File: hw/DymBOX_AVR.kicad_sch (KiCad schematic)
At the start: 45 parts, among them J4 DS18B20, J5 Conn_02x05_Odd_Even, J6 Conn_01x01_Pin, J7 Conn_01x01_Pin, J8 Conn_01x01_Pin, J9 Conn_01x01_Pin, K1 RT314A24, Q1 BC327, Q2 BC327, Q3 BS170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

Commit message: prace
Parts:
- removed J7, J8, J9: Conn_01x01_Pin, 2pkstartup:TRM2_62409-1_TEC, symbol 2pkstartup:FST
- added J1, J2, J3: Conn_01x01_Pin, 2pkstartup:faston_6.3, symbol 2pkstartup:FST
- J6: footprint 2pkstartup:TRM2_62409-1_TEC -> 2pkstartup:faston_6.3
- SW1: footprint Rotary_Encoder:RotaryEncoder_Alps_EC12E-Switch_Vertical_H20mm_CircularMountingHoles -> 2pkstartup:RotaryEncoder_Alps_EC12E-Switch_Vertical_H20mm_CircularMountingHoles
- U3: footprint Package_TO_SOT_THT:TO-220-3_Horizontal_TabDown -> Package_TO_SOT_THT:TO-220-3_Vertical
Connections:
- net at K1.11: now also J3.1 (Pin_1)
- net at TR1.5: now also J1.1 (Pin_1); no longer J6.1 (Pin_1)
- net at TR1.1: now also J2.1 (Pin_1)
- net at K1.14: now also J6.1 (Pin_1)

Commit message: uprava a více
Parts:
- removed J4: DS18B20, Connector_Wire:SolderWire-0.127sqmm_1x03_P3.7mm_D0.48mm_OD1mm, symbol Connector:Conn_01x03_Pin
- removed SW1: RotaryEncoder_Switch, 2pkstartup:RotaryEncoder_Alps_EC12E-Switch_Vertical_H20mm_CircularMountingHoles, symbol Device:RotaryEncoder_Switch
- added J4: Screw_Terminal_01x03, TerminalBlock_Phoenix:TerminalBlock_Phoenix_PT-1,5-3-3.5-H_1x03_P3.50mm_Horizontal, symbol Connector:Screw_Terminal_01x03
- added J7: Screw_Terminal_01x02, TerminalBlock_Phoenix:TerminalBlock_Phoenix_PT-1,5-2-3.5-H_1x02_P3.50mm_Horizontal, symbol Connector:Screw_Terminal_01x02
- added SW2: RotaryEncoder_Switch, 2pkstartup:RotaryEncoder_Alps_EC12E-Switch_Vertical_H20mm_CircularMountingHoles, symbol 2pkstartup:RotaryEncoder_Switch
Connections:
- net +12V: now also J7.1 (Pin_1)
- net +5V: now also J4.3 (Pin_3)
- net BTN: now also SW2.S1
- net CLK: now also SW2.A
- net DT: now also SW2.B
- net GND: now also J4.1 (Pin_1), SW2.C, SW2.S2
- net at D1.2 (A), Q3.1 (D): now also J7.2 (Pin_2)
- net at R13.1, U1.28 (PC5): now also J4.2 (Pin_2)
- net at Q1.1 (C): now also U2.8 (CA3); no longer U2.6 (CA4)
- net at Q2.1 (C): now also U2.9 (CA2); no longer U2.8 (CA3)
- net at Q5.1 (C): now also U2.12 (CA1); no longer U2.9 (CA2)
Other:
- moved on the sheet: Q1, Q2, Q5, R11, R12

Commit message: AP63005
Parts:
- removed U2: CA56-12EWA, Display_7Segment:CA56-12EWA, symbol Display_Character:CA56-12EWA
- added U2: FYT-5631BUHR-21, 2pkstartup:FYT-5631BUHR-21, symbol 2pkstartup:FYT-5631BUHR-21
- C1, C2: footprint Capacitor_THT:CP_Radial_D13.0mm_P5.00mm -> Capacitor_THT:CP_Radial_D16.0mm_P7.50mm
- U3: footprint Package_TO_SOT_THT:TO-220-3_Vertical -> Package_TO_SOT_THT:TO-220-3_Horizontal_TabDown
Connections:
- net at R7.2: now also U2.3 (DPX)
- net at R6.2: now also U2.2 (d)
- net at R8.2: now also U2.10 (f)
- net at R9.2: now also U2.5 (g)
- net at R2.2: now also U2.11 (a)
- net at R3.2: now also U2.7 (b)
- net at R5.2: now also U2.1 (e)
- net at R4.2: now also U2.4 (c)
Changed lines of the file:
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@@
 			)
 		)
-		(property "Footprint" "Package_TO_SOT_THT:TO-220-3_Vertical"
+		(property "Footprint" "Package_TO_SOT_THT:TO-220-3_Horizontal_TabDown"
 			(at 53.975 64.77 0)
 			(show_name no)
@@
 			)
 		)
-		(property "Footprint" "Capacitor_THT:CP_Radial_D13.0mm_P5.00mm"
+		(property "Footprint" "Capacitor_THT:CP_Radial_D16.0mm_P7.50mm"
 			(at 40.3352 68.58 0)
 			(hide yes)
@@
 			)
 		)
-		(property "Footprint" "Capacitor_THT:CP_Radial_D13.0mm_P5.00mm"
+		(property "Footprint" "Capacitor_THT:CP_Radial_D16.0mm_P7.50mm"
 			(at 61.9252 68.58 0)
 			(hide yes)
@@
 	)
 	(symbol
-		(lib_id "Display_Character:CA56-12EWA")
-		(at 139.7 43.18 0)
-		(unit 1)
-		(body_style 1)
-		(exclude_from_sim no)
-		(in_bom yes)
-		(on_board yes)
-		(in_pos_files yes)
-		(dnp no)
-		(fields_autoplaced yes)
-		(property "Reference" "U2"
-			(at 139.7 25.4 0)
-			(show_name no)
-			(do_not_autoplace no)
-			(effects
-				(font
-					(size 1.27 1.27)
-				)
-			)
-		)
-		(property "Value" "CA56-12EWA"
-			(at 139.7 27.94 0)
-			(show_name no)
-			(do_not_autoplace no)
-			(effects
-				(font
-					(size 1.27 1.27)
-				)
-			)
-		)
-		(property "Footprint" "Display_7Segment:CA56-12EWA"
-			(at 139.7 58.42 0)
-			(hide yes)
-			(show_name no)
-			(do_not_autoplace no)
-			(effects
-				(font
-					(size 1.27 1.27)
-				)
-			)
-		)
-		(property "Datasheet" "http://www.kingbrightusa.com/images/catalog/SPEC/CA56-12EWA.pdf"
-			(at 128.778 42.418 0)
-			(hide yes)
-			(show_name no)
-			(do_not_autoplace no)
-			(effects
-				(font
-					(size 1.27 1.27)
-				)
-			)
-		)
-		(property "Description" "4 digit 7 segment high efficiency red LED, common anode"
-			(at 139.7 43.18 0)
-			(hide yes)
-			(show_name no)
-			(do_not_autoplace no)
-			(effects
-				(font
-					(size 1.27 1.27)
-				)
-			)
-		)
-		(pin "10"
-		)
-		(pin "3"
-		)
-		(pin "11"
-		)
-		(pin "9"
-		)
-		(pin "8"
-		)
-		(pin "12"
-		)
-		(pin "6"
-		)
-		(pin "4"
-		)
-		(pin "7"
-		)
-		(pin "5"
-		)
-		(pin "1"
-		)
-		(pin "2"
-		)
-		(instances
-			(project "DymBOX_AVR"
-				(path "/586f9677-488d-4753-8c82-bcf4ec642766"
-					(reference "U2")
-					(unit 1)
-				)
-			)
-		)
-	)
-	(symbol
 		(lib_id "Device:R")
 		(at 118.11 110.49 180)
@@
 					(unit 1)
 				)
+			)
+		)
+	)
+	(symbol
+		(lib_id "2pkstartup:FYT-5631BUHR-21")
+		(at 139.7 43.18 0)
+		(unit 1)
+		(body_style 1)
+		(exclude_from_sim no)
+		(in_bom yes)
+		(on_board yes)
+		(in_pos_files yes)
+		(dnp no)
+		(fields_autoplaced yes)
+		(property "Reference" "U2"
+			(at 133.985 25.4 0)
+			(show_name no)
+			(do_not_autoplace no)
+			(effects
+				(font
+					(size 1.27 1.27)
+				)
+			)
+		)
+		(property "Value" "FYT-5631BUHR-21"
+			(at 133.985 27.94 0)
+			(show_name no)
+			(do_not_autoplace no)
+			(effects
+				(font
+					(size 1.27 1.27)
+				)
+			)
+		)
+		(property "Footprint" "2pkstartup:FYT-5631BUHR-21"
+			(at 139.7 58.42 0)
+			(hide yes)
+			(show_name no)
+			(do_not_autoplace no)
+			(effects
+				(font
+					(size 1.27 1.27)
+				)
+			)
+		)
+		(property "Datasheet" "https://cetest02.cn-bj.ufileos.com/100001_2003185297/20%20FYT-5631A-BX-XX.pdf"
+			(at 128.778 42.418 0)
+			(hide yes)
+			(show_name no)
+			(do_not_autoplace no)
+			(effects
+				(font
+					(size 1.27 1.27)
+				)
+			)
+		)
+		(property "Description" "3 digit 7 segment high efficiency red LED, common anode"
+			(at 139.7 43.18 0)
+			(hide yes)
+			(show_name no)
+			(do_not_autoplace no)
+			(effects
+				(font
+					(size 1.27 1.27)
+				)
+			)
+		)
+		(pin "3"
+		)
+		(pin "1"
+		)
+		(pin "4"
+		)
+		(pin "2"
+		)
+		(pin "9"
+		)
+		(pin "5"
+		)
+		(pin "8"
+		)
+		(pin "7"
+		)
+		(pin "10"
+		)
+		(pin "6"
+		)
+		(pin "11"
+		)
+		(pin "12"
+		)
+		(instances
+			(project "DymBOX_AVR"
+				(path "/586f9677-488d-4753-8c82-bcf4ec642766"
+					(reference "U2")
+					(unit 1)
+				)

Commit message: AP63005
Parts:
- removed C1, C2: C_Polarized, Capacitor_THT:CP_Radial_D16.0mm_P7.50mm, symbol Device:C_Polarized
- removed C3: C_Small, Capacitor_THT:C_Disc_D5.0mm_W2.5mm_P5.00mm, symbol Device:C_Small
- removed U3: L7805, Package_TO_SOT_THT:TO-220-3_Horizontal_TabDown, symbol Regulator_Linear:L7805
- added C1: 3m3F, Capacitor_THT:CP_Radial_D16.0mm_P7.50mm, symbol Device:C_Polarized_Small
- added C10, C9: 22uF, Capacitor_SMD:C_0805_2012Metric_Pad1.18x1.45mm_HandSolder, symbol Device:C_Small
- added C2: C_Small, Capacitor_SMD:C_1206_3216Metric_Pad1.33x1.80mm_HandSolder, symbol Device:C_Small
- added C8: 100nF, Capacitor_SMD:C_0805_2012Metric_Pad1.18x1.45mm_HandSolder, symbol Device:C_Small
- added L1: 4u7H, Inductor_SMD:L_1210_3225Metric_Pad1.42x2.65mm_HandSolder, symbol Device:L_Small
- added U4: AP63205WU, Package_TO_SOT_SMD:TSOT-23-6, symbol Regulator_Switching:AP63205WU
- C4, C5, C6: footprint Capacitor_THT:C_Disc_D5.0mm_W2.5mm_P5.00mm -> Capacitor_SMD:C_0805_2012Metric_Pad1.18x1.45mm_HandSolder
- TR1: footprint Transformer_THT:Transformer_Breve_TEZ-38x45 -> 2pkstartup:Transformer_Breve_TEZ-38x45
- Y1: footprint Crystal:Crystal_HC49-U_Vertical -> Crystal:Crystal_SMD_HC49-SD_HandSoldering
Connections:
- net +12V: now also C1.1, C2.1, U4.2 (EN), U4.3 (IN)
- net +5V: now also C10.1, C9.1, L1.2, U4.1 (FB)
- net GND: now also C1.2, C10.2, C2.2, C9.2, U4.4 (GND)
- net at Q1.1 (C): now also U2.8 (CA3)
- net at Q2.1 (C): now also U2.9 (CA2)
- net at Q5.1 (C): now also U2.12 (CA1)
- new net: C8.1, L1.1, U4.5 (SW)
- new net: C8.2, U4.6 (BST)
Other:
- moved on the sheet: Q1, Q2, Q5, R10, R11, R12

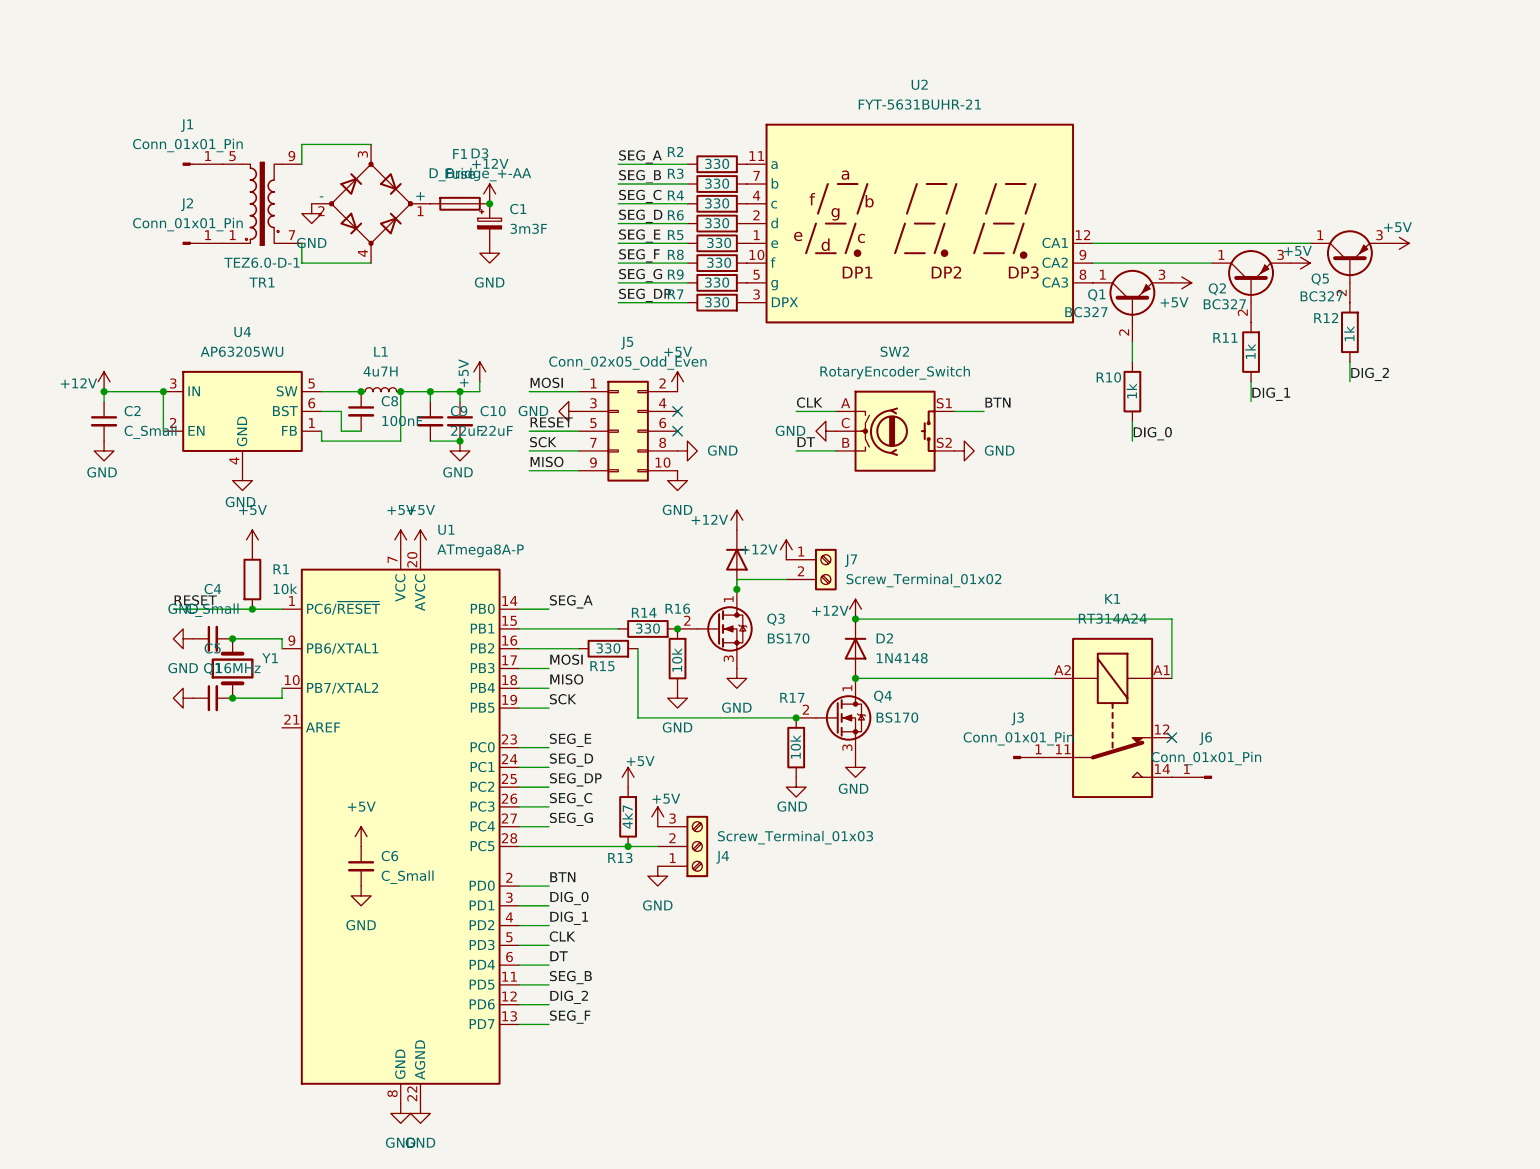
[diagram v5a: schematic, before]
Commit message: pojistka16A a další
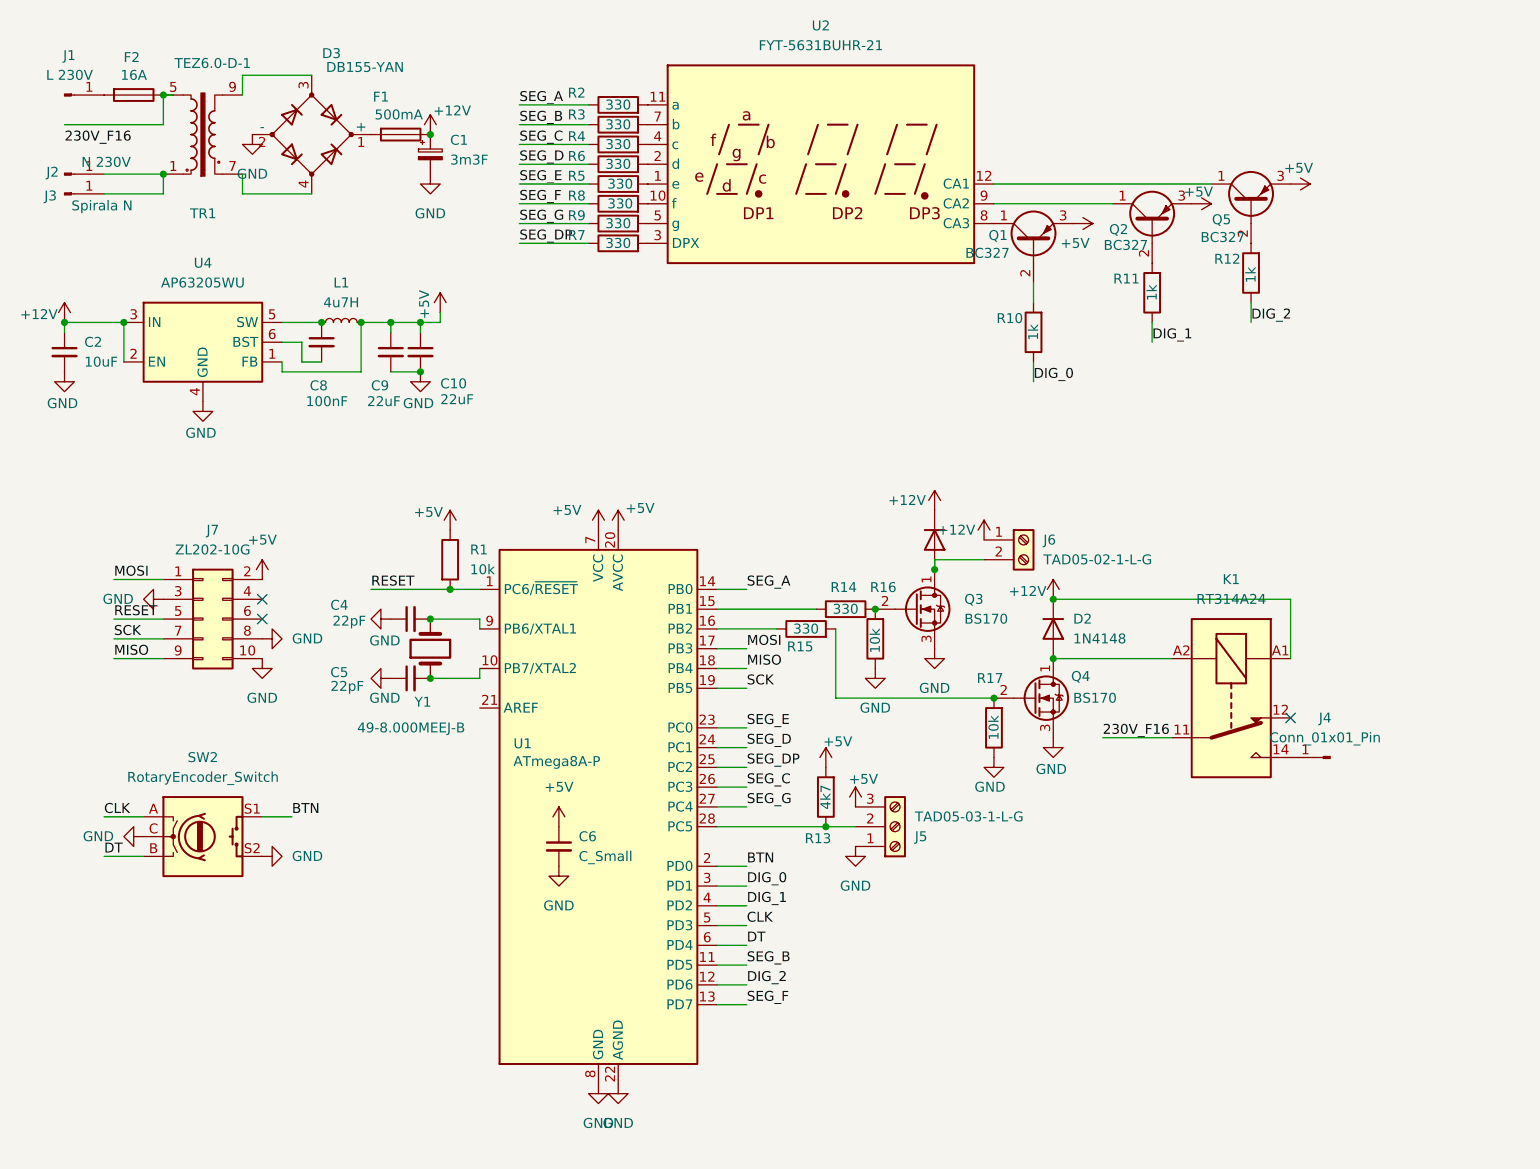
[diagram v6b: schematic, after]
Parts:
- added F2: 16A, Fuse:Fuseholder_Clip-5x20mm_Littelfuse_111_Inline_P20.00x5.00mm_D1.05mm_Horizontal, symbol Device:Fuse
- C2: value C_Small -> 10uF
- C4: value C_Small -> 22pF
- C5: value Q1 -> 22pF
- D3: value D_Bridge_+-AA -> DB155-YAN
- F1: value Fuse -> 500mA
- J1: value Conn_01x01_Pin -> L 230V
- J2: value Conn_01x01_Pin -> N 230V
- J3: value Conn_01x01_Pin -> Spirala N
- J5: renamed from J4; value Screw_Terminal_01x03 -> TAD05-03-1-L-G
- J6: renamed from J7; value Screw_Terminal_01x02 -> TAD05-02-1-L-G
- J7: renamed from J5; value Conn_02x05_Odd_Even -> ZL202-10G
- Y1: value 16MHz -> 49-8.000MEEJ-B; footprint Crystal:Crystal_SMD_HC49-SD_HandSoldering -> Crystal:Crystal_HC49-U_Vertical
- renumbered J6 to J4
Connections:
- net at J2.1 (Pin_1), TR1.1: now also J3.1 (Pin_1)
- net at TR1.5: now also F2.1; no longer J1.1 (Pin_1)
- net 230V_F16: now reaches K1.11
- net 230V_F16: no longer J3.1 (Pin_1)
- new net: F2.2, J1.1 (Pin_1)
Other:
- moved on the sheet: C1, C10, C2, C4, C5, C6, C8, C9, D2, D3, F1, J1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
